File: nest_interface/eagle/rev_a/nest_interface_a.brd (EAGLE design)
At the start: 105.4 x 110.5 mm, 109 parts, among them J1 MOLEX_MICRO_USB_B_047346, J11 CONN_BLOCK_2, J12 CONN_BLOCK_2, J13 CONN_BLOCK_2, J14 CONN_BLOCK_2, J15 CONN_BLOCK_2, J17 CONN_BLOCK_3, J2 CONN_BLOCK_2, J23 CONN_BLOCK_8, J24 CONN_BLOCK_8, J25 MOLEX_MICRO_USB_B_047346, J3 CONN_BLOCK_3, J30 PINH2X12, J4 PJ-036A-SMT, J5 CONN_BLOCK_8, J6 CONN_BLOCK_8, J7 CONN_BLOCK_7, J8 CONN_BLOCK_7, U1 FT232RL, U10 ALD1107, U11 ALD1107, U2 EPIC-CORE_A, U20 MSP430F1611IPM, U3 MPC1825, U4 PCA9575, U5 PCA9575, U6 FT232RL, U7 TC1262, U8 ALD1107, U9 ALD1107, Y1 FC-135_32.768KA-A3

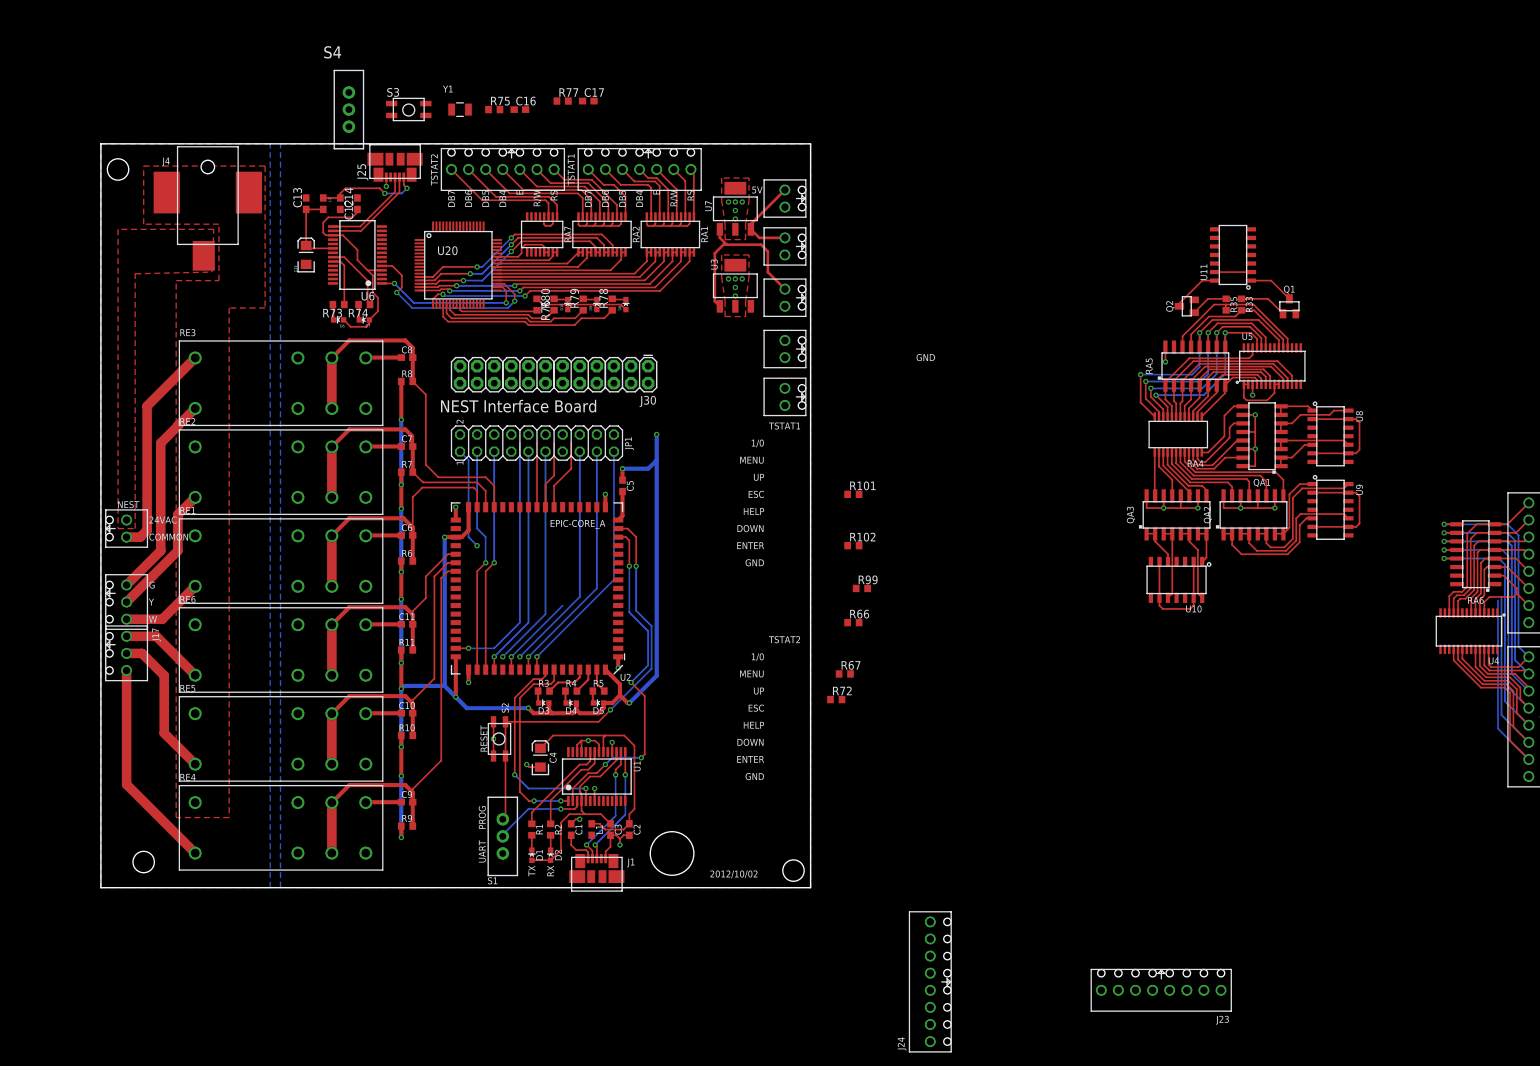
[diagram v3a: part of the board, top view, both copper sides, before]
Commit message: cleaned up the nib schematic
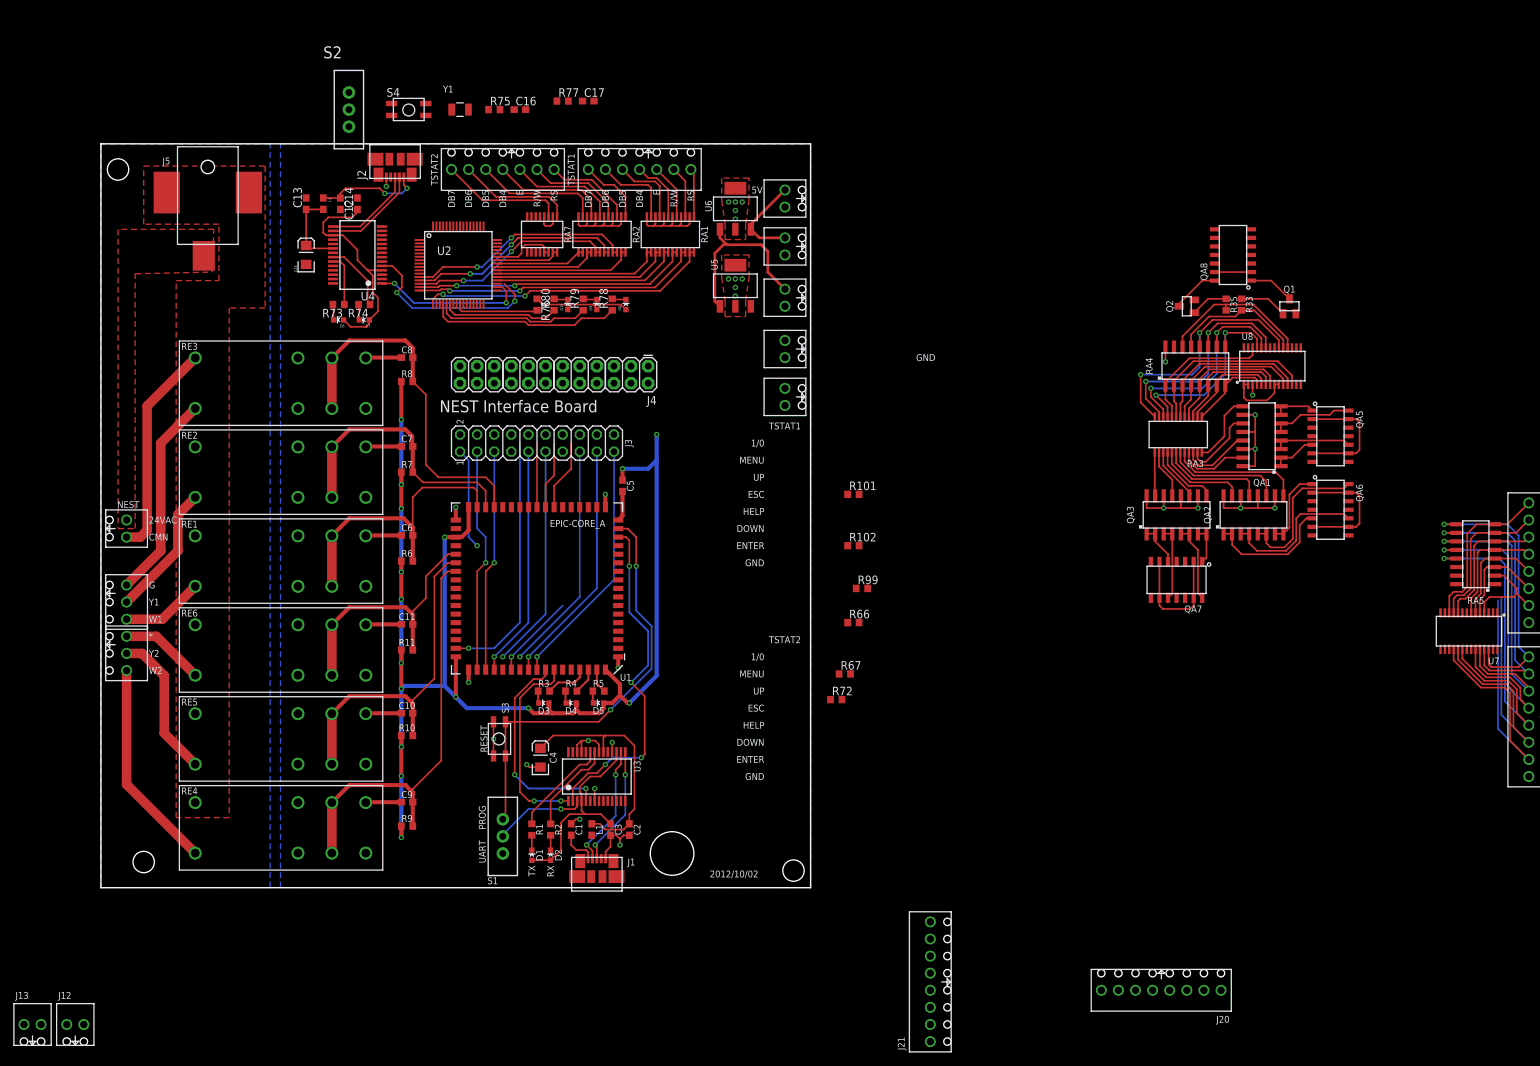
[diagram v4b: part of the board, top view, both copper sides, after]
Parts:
- removed J25: MOLEX_MICRO_USB_B_047346, nest_interface:MOLEX_MICRO_USB_B_047346
- removed J30: PINH2X12, SparkFun:2X12
- removed JP1: (no value), pinhead:2X10
- removed RA6: 766161104GP, nest_interface:SOIC-16
- removed U20: MSP430F1611IPM, hijack:PM/PAG64
- added J10, J9: CONN_BLOCK_2, nest_interface:CONN_BLOCK_2
- added J16: CONN_BLOCK_7, nest_interface:CONN_BLOCK_7
- added J18, J19: CONN_BLOCK_8, nest_interface:CONN_BLOCK_8
- added QA5: ALD1107, nest_interface:SOIC-14
- added RA3: VSSR2403103, nest_interface:LSSOP-24
- J14, J15: value CONN_BLOCK_2 -> CONN_BLOCK_3; device nest_interface:CONN_BLOCK_2 -> nest_interface:CONN_BLOCK_3
- J17: value CONN_BLOCK_3 -> CONN_BLOCK_7; device nest_interface:CONN_BLOCK_3 -> nest_interface:CONN_BLOCK_7
- J2: value CONN_BLOCK_2 -> MOLEX_MICRO_USB_B_047346; device nest_interface:CONN_BLOCK_2 -> nest_interface:MOLEX_MICRO_USB_B_047346
- J3: value CONN_BLOCK_3 -> (none); device nest_interface:CONN_BLOCK_3 -> pinhead:2X10
- J4: value PJ-036A-SMT -> PINH2X12; device nest_interface:PJ-0361-SMT -> SparkFun:2X12
- J5: value CONN_BLOCK_8 -> PJ-036A-SMT; device nest_interface:CONN_BLOCK_8 -> nest_interface:PJ-0361-SMT
- J6: value CONN_BLOCK_8 -> CONN_BLOCK_2; device nest_interface:CONN_BLOCK_8 -> nest_interface:CONN_BLOCK_2
- J7, J8: value CONN_BLOCK_7 -> CONN_BLOCK_2; device nest_interface:CONN_BLOCK_7 -> nest_interface:CONN_BLOCK_2
- RA4: value VSSR2403103 -> 766161104GP; device nest_interface:LSSOP-24 -> nest_interface:SOIC-16
- S2: value EVQP2 -> (none); device berkeley-epic:EVQP2 -> SparkFun:SWITCH-SPDT
- S4: value (none) -> EVQP2; device SparkFun:SWITCH-SPDT -> berkeley-epic:EVQP2
- U1: value FT232RL -> EPIC-CORE_A; device ftdichip:SSOP28 -> berkeley-epic:EPIC-LCC68
- U2: value EPIC-CORE_A -> MSP430F1611IPM; device berkeley-epic:EPIC-LCC68 -> hijack:PM/PAG64
- U3: value MPC1825 -> FT232RL; device nest_interface:SOT-223-3 -> ftdichip:SSOP28
- U4: value PCA9575 -> FT232RL; device nest_interface:TSSOP28 -> ftdichip:SSOP28
- U5: value PCA9575 -> MPC1825; device nest_interface:TSSOP28 -> nest_interface:SOT-223-3
- U6: value FT232RL -> TC1262; device ftdichip:SSOP28 -> nest_interface:SOT-223-3
- U7: value TC1262 -> PCA9575; device nest_interface:SOT-223-3 -> nest_interface:TSSOP28
- U8: value ALD1107 -> PCA9575; device nest_interface:SOIC-14 -> nest_interface:TSSOP28
- moved J6 210.1 mm to (3.81, 53.3), turned to 270 degrees
- moved J5 203.8 mm to (15.9, 103.3), turned to 270 degrees
- moved U4 174.3 mm to (38.1, 94.0), turned to 90 degrees
- moved J12 161.7 mm to (-3.81, -20.3), turned to 0 degrees
- moved J13 160.8 mm to (-10.2, -20.3), turned to 0 degrees
- moved U7 125.7 mm to (203.2, 38.1), turned to 180 degrees
- moved J15 104.9 mm to (3.81, 34.8), turned to 270 degrees
- moved J14 104.8 mm to (3.81, 42.4), turned to 270 degrees
- moved S2 96.1 mm to (36.8, 115.6), turned to 0 degrees
- moved S3 94.4 mm to (59.2, 22.1), turned to 270 degrees
- moved J17 91.0 mm to (59.7, 106.7), turned to 180 degrees
- moved U5 80.6 mm to (94.2, 89.4)
- moved U3 75.7 mm to (73.7, 16.5)
- moved J2 67.8 mm to (43.7, 108.2)
- moved J3 65.4 mm to (64.8, 66.0), turned to 0 degrees
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- renumbered J23 to J20, J24 to J21, U10 to QA7, U11 to QA8, U9 to QA6
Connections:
- new net TSTAT1_SPEAKER_IN: J12.2
- new net TSTAT1_SPEAKER_OUT: J12.1
- new net TSTAT2_SPEAKER_IN: J13.2
- new net TSTAT2_SPEAKER_OUT: J13.1
- net #KEYPAD_ENABLE: now also QA5.13, QA5.2, QA5.6, QA5.9, U1.P$4; no longer U2.P$4, U8.13, U8.2, U8.6, U8.9
- net 5.6V_SUPPLY: now also J7.2, U5.1, U6.1; no longer J11.2, U3.1, U7.1
- net 5V: now also J8.2, J9.2, U6.3; no longer J12.2, J13.2, U7.3
- net COMMON: now also J5.2, J5.3, J6.2; no longer J2.2, J4.2, J4.3
- net COOLING1_PIN: now also U1.P$32; no longer U2.P$32
- net COOLING2_PIN: now also U1.P$40; no longer U2.P$40
- net EPIC_ADC1: now also J3.18, U1.P$20; no longer JP1.18, U2.P$20
- net EPIC_ADC2: now also J3.16, U1.P$21; no longer JP1.16, U2.P$21
- net EPIC_ADC3: now also J3.14, U1.P$22; no longer JP1.14, U2.P$22
- net EPIC_ADC4: now also J3.12, U1.P$23; no longer JP1.12, U2.P$23
- net EPIC_ADC5: now also J3.10, U1.P$24; no longer JP1.10, U2.P$24
- net EPIC_ADC6/DAC0: now also J3.8, U1.P$25; no longer JP1.8, U2.P$25
- net EPIC_ADC7/DAC1: now also J3.6, U1.P$26; no longer JP1.6, U2.P$26
- net EPIC_MISO0: now also J3.13, U1.P$57; no longer JP1.13, U2.P$57
- net EPIC_P2.0: now also J3.1, U1.P$38; no longer JP1.1, U2.P$38
- net EPIC_P2.4: now also J3.5, U1.P$54; no longer JP1.5, U2.P$54
- net EPIC_P2.7: now also J3.3, U1.P$53; no longer JP1.3, U2.P$53
- net EPIC_P5.7: now also J3.7, U1.P$9; no longer JP1.7, U2.P$9
- net EPIC_STE0: now also J3.9, U1.P$55; no longer JP1.9, U2.P$55
- net EPIC_UART0RX: now also J3.19, U1.P$60; no longer JP1.19, U2.P$60
- net EPIC_UART0TX: now also J3.17, U1.P$59; no longer JP1.17, U2.P$59
- net FAN_PIN: now also U1.P$31; no longer U2.P$31
- net G: now also J14.1; no longer J3.1
- net GND: now also J10.1, J18.1, J19.1, J2.GND, J3.20, J7.1, J8.1, J9.1, QA5.4, RA4.16, S4.P$1, S4.P$3, U1.P$1, U1.P$18, U1.P$35, U1.P$52, U2.10, U2.11, U2.53, U2.62, U2.63, U3.18, U3.21, U3.25, U3.26, U3.7, U4.18, U4.21, U4.25, U4.26, U4.7, U5.2, U5.4, U6.2, U6.4, U7.13, U7.16, U7.17, U7.22, U8.15, U8.16, U8.22; no longer J12.1, J13.1, J14.1, J15.1, J25.GND, J5.1, J6.1, JP1.20, RA5.16, S2.P$1, S2.P$3, U1.18, U1.21, U1.25, U1.26, U1.7, U2.P$1, U2.P$18, U2.P$35, U2.P$52, U20.10, U20.11, U20.53, U20.62, U20.63, U3.2, U3.4, U4.13, U4.16, U4.17, U4.22, U5.15, U5.16, U5.22, U6.18, U6.21, U6.25, U6.26, U6.7, U7.2, U7.4, U8.4
- net HEATING1_PIN: now also U1.P$33; no longer U2.P$33
- net HEATING2_PIN: now also U1.P$41; no longer U2.P$41
- net I2C_SCL: now also J3.15, U1.P$58, U2.31, U7.28, U8.28; no longer JP1.15, U2.P$58, U20.31, U4.28, U5.28
- net I2C_SDA: now also J3.11, U1.P$56, U2.29, U7.27, U8.27; no longer JP1.11, U2.P$56, U20.29, U4.27, U5.27
- net LCDP_MISO0: now also J4.16, U2.30; no longer J30.16, U20.30
- net LCDP_P2.4: now also J4.4, U2.24; no longer J30.4, U20.24
- net LCDP_P2.7: now also U2.27; no longer U20.27
- net LCDP_STE0: now also J4.18, U2.28; no longer J30.18, U20.28
- net LCDP_URXD0: now also J4.12, U2.33; no longer J30.12, U20.33
- net LCDP_UTXD0: now also J4.14, U2.32; no longer J30.14, U20.32
- net N$10: now also U3.23; no longer U1.23
- net N$11: now also U3.22; no longer U1.22
- net N$12: now also U1.P$61, U3.5; no longer U1.5, U2.P$61
- net N$14: now also U1.P$15, U3.2; no longer U1.2, U2.P$15
- net N$15: now also U3.17, U3.4; no longer U1.17, U1.4
- net N$16: now also RA3.23; no longer RA4.23
- net N$17: now also RA3.18; no longer RA4.18
- net N$18: now also U1.P$17; no longer U2.P$17
- net N$22: now also U1.P$67; no longer U2.P$67
- net N$23: now also U1.P$66; no longer U2.P$66
- net N$24: now also U1.P$65; no longer U2.P$65
- net N$25: now also RA3.19; no longer RA4.19
- net N$26: now also RA3.20; no longer RA4.20
- net N$28: now also RA3.13; no longer RA4.13
- net N$29: now also RA3.14; no longer RA4.14
- net N$3: now also U3.16; no longer U1.16
- net N$30: now also RA3.15; no longer RA4.15
- net N$37: now also RA3.24; no longer RA4.24
- net N$38: now also U2.8; no longer U20.8
- net N$39: now also J2.VCC; no longer J25.VCC
- net N$4: now also U3.15; no longer U1.15
- net N$40: now also J2.D-, U4.16; no longer J25.D-, U6.16
- net N$41: now also J2.D+, U4.15; no longer J25.D+, U6.15
- net N$43: now also U4.20; no longer U6.20
- net N$44: now also U4.23; no longer U6.23
- net N$45: now also U4.22; no longer U6.22
- net N$48: now also U2.35, U4.1; no longer U20.34, U6.1
- net N$49: now also U2.34, U4.5; no longer U20.35, U6.5
- net N$5: now also RA3.17; no longer RA4.17
- net N$50: now also U2.57, U4.2; no longer U20.57, U6.2
- net N$51: now also U4.17, U4.4; no longer U6.17, U6.4
- net N$52: now also U2.9; no longer U20.9
- net N$54: now also U2.25; no longer U20.25
- net N$56: now also U2.21; no longer U20.21
- net N$57: now also U2.22; no longer U20.22
- net N$58: now also RA3.22; no longer RA4.22
- net N$6: now also U3.20; no longer U1.20
- net N$60: now also RA3.21; no longer RA4.21
- net N$65: now also RA3.16; no longer RA4.16
- net N$8: now also U2.20; no longer U20.20
- net N$9: now also U1.P$62, U3.1; no longer U1.1, U2.P$62
- net P1.6: now also J4.10, U2.18; no longer J30.10, U20.18
- net P1.7: now also J4.8, U2.19; no longer J30.8, U20.19
- net P2.3: now also J4.6, U2.23; no longer J30.6, U20.23
- net P2.6: now also J4.2, U2.26; no longer J30.2, U20.26
- net P5.0: now also J4.1, U2.44; no longer J30.1, U20.44
- net P5.1: now also J4.3, U2.45; no longer J30.3, U20.45
- net P5.2: now also J4.5, U2.46; no longer J30.5, U20.46
- net P5.3: now also J4.7, U2.47; no longer J30.7, U20.47
- net P5.4: now also J4.9, U2.48; no longer J30.9, U20.48
- net P5.5: now also U2.49; no longer U20.49
- net P5.6: now also J4.11, U2.50; no longer J30.11, U20.50
- net P5.7: now also J4.13, U2.51; no longer J30.13, U20.51
- net P6.0: now also J4.15, U2.59; no longer J30.15, U20.59
- net P6.1: now also J4.17, U2.60; no longer J30.17, U20.60
- net P6.2: now also J4.19, U2.61; no longer J30.19, U20.61
- net P6.3: now also J4.21, U2.2; no longer J30.21, U20.2
- net P6.4: now also J4.23, U2.3; no longer J30.23, U20.3
- net P6.5: now also J4.24, U2.4; no longer J30.24, U20.4
- net P6.6: now also J4.22, U2.5; no longer J30.22, U20.5
- net P6.7: now also J4.20, U2.6; no longer J30.20, U20.6
- net RADIO_SFD: now also J3.4, U1.P$50; no longer JP1.4, U2.P$50
- net RH: now also J5.1, J6.1; no longer J2.1, J4.1
- net RST: now also S3.P$2, S3.P$4, U1.P$16; no longer S2.P$2, S2.P$4, U2.P$16
- net RST1: now also S2.1, S4.P$2, S4.P$4, U2.58; no longer S3.P$2, S3.P$4, S4.1, U20.58
- net RST_USB: now also U3.3; no longer U1.3
- net RST_USB1: now also S2.2, U4.3; no longer S4.2, U6.3
- net STAR: now also J15.1; no longer J17.1
- net STAR_PIN: now also U1.P$39; no longer U2.P$39
- net TSTAT1_DOWN_IN: now also J18.3, RA5.3, U7.5; no longer J5.3, RA6.3, U4.5
- net TSTAT1_DOWN_OUT_PIN: now also RA3.6, RA4.3, U8.11; no longer RA4.6, RA5.3, U5.11
- net TSTAT1_ENTER_IN: now also J18.2, RA5.2, U7.4; no longer J5.2, RA6.2, U4.4
- net TSTAT1_ENTER_OUT_PIN: now also RA3.7, RA4.2, U8.12; no longer RA4.7, RA5.2, U5.12
- net TSTAT1_ESC_IN: now also J18.5, QA5.7, RA5.5, U7.7; no longer J5.5, RA6.5, U4.7, U8.7
- net TSTAT1_ESC_OUT: now also QA5.5; no longer U8.5
- net TSTAT1_ESC_OUT_PIN: now also RA3.4, RA4.5, U8.7; no longer RA4.4, RA5.5, U5.7
- net TSTAT1_HELP_IN: now also J18.4, RA5.4, U7.6; no longer J5.4, RA6.4, U4.6
- net TSTAT1_HELP_OUT_PIN: now also RA3.5, RA4.4, U8.10; no longer RA4.5, RA5.4, U5.10
- net TSTAT1_LCD_DB4: now also J16.4; no longer J7.4
- net TSTAT1_LCD_DB4_PIN: now also U2.36; no longer U20.36
- net TSTAT1_LCD_DB5: now also J16.5; no longer J7.5
- net TSTAT1_LCD_DB5_PIN: now also U2.37; no longer U20.37
- net TSTAT1_LCD_DB6: now also J16.6; no longer J7.6
- net TSTAT1_LCD_DB6_PIN: now also U2.38; no longer U20.38
- net TSTAT1_LCD_DB7: now also J16.7; no longer J7.7
- net TSTAT1_LCD_DB7_PIN: now also U2.39; no longer U20.39
- net TSTAT1_LCD_E: now also J16.3; no longer J7.3
- net TSTAT1_LCD_E_PIN: now also U2.15; no longer U20.15
- net TSTAT1_LCD_R/W: now also J16.2; no longer J7.2
- net TSTAT1_LCD_R/W_PIN: now also U2.16; no longer U20.16
- net TSTAT1_LCD_RS: now also J16.1; no longer J7.1
- net TSTAT1_LCD_RS_PIN: now also U2.17; no longer U20.17
- net TSTAT1_MENU_IN: now also J18.7, QA5.12, RA5.7, U7.11; no longer J5.7, RA6.7, U4.11, U8.12
- net TSTAT1_MENU_OUT: now also QA5.14; no longer U8.14
- net TSTAT1_MENU_OUT_PIN: now also RA3.2, RA4.7, U8.5; no longer RA4.2, RA5.7, U5.5
- net TSTAT1_ON/OFF_IN: now also J18.8, QA5.3, RA5.8, U7.12; no longer J5.8, RA6.8, U4.12, U8.3
- net TSTAT1_ON/OFF_OUT: now also QA5.1; no longer U8.1
- net TSTAT1_ON/OFF_OUT_PIN: now also RA3.1, RA4.8, U8.4; no longer RA4.1, RA5.8, U5.4
- net TSTAT1_UP_IN: now also J18.6, QA5.8, RA5.6, U7.10; no longer J5.6, RA6.6, U4.10, U8.8
- net TSTAT1_UP_OUT: now also QA5.10; no longer U8.10
- net TSTAT1_UP_OUT_PIN: now also RA3.3, RA4.6, U8.6; no longer RA4.3, RA5.6, U5.6
- net TSTAT2_DOWN_IN: now also J19.3, RA5.14, U7.19; no longer J6.3, RA6.14, U4.19
- net TSTAT2_DOWN_OUT_PIN: now also RA4.13, U8.19; no longer RA5.13, U5.19
- net TSTAT2_ENTER_IN: now also J19.2, RA5.15, U7.18; no longer J6.2, RA6.15, U4.18
- net TSTAT2_ENTER_OUT_PIN: now also RA4.14, U8.18; no longer RA5.14, U5.18
- net TSTAT2_ESC_IN: now also J19.5, RA5.12, U7.23; no longer J6.5, RA6.12, U4.23
- net TSTAT2_ESC_OUT_PIN: now also RA3.11, U8.23; no longer RA5.11, U5.23
- net TSTAT2_HELP_IN: now also J19.4, RA5.13, U7.20; no longer J6.4, RA6.13, U4.20
- net TSTAT2_HELP_OUT_PIN: now also RA3.12, U8.20; no longer RA5.12, U5.20
- net TSTAT2_LCD_DB4: now also J17.4; no longer J8.4
- net TSTAT2_LCD_DB4_PIN: now also U2.40; no longer U20.40
- net TSTAT2_LCD_DB5: now also J17.5; no longer J8.5
- net TSTAT2_LCD_DB5_PIN: now also U2.41; no longer U20.41
- net TSTAT2_LCD_DB6: now also J17.6; no longer J8.6
- net TSTAT2_LCD_DB6_PIN: now also U2.42; no longer U20.42
- net TSTAT2_LCD_DB7: now also J17.7; no longer J8.7
- net TSTAT2_LCD_DB7_PIN: now also U2.43; no longer U20.43
- net TSTAT2_LCD_E: now also J17.3; no longer J8.3
- net TSTAT2_LCD_E_PIN: now also U2.14; no longer U20.14
- net TSTAT2_LCD_R/W: now also J17.2; no longer J8.2
- net TSTAT2_LCD_R/W_PIN: now also U2.13; no longer U20.13
- net TSTAT2_LCD_RS: now also J17.1; no longer J8.1
- net TSTAT2_LCD_RS_PIN: now also U2.12; no longer U20.12
- net TSTAT2_MENU_IN: now also J19.7, RA5.10, U7.25; no longer J6.7, RA6.10, U4.25
- net TSTAT2_MENU_OUT_PIN: now also RA3.9, U8.25; no longer RA5.9, U5.25
- net TSTAT2_ON/OFF_IN: now also J19.8, RA5.9, U7.26; no longer J6.8, RA6.9, U4.26
- net TSTAT2_ON/OFF_OUT_PIN: now also RA3.8, RA4.1, U8.26; no longer RA4.8, RA5.1, U5.26
- net TSTAT2_UP_IN: now also J19.6, RA5.11, U7.24; no longer J6.6, RA6.11, U4.24
- net TSTAT2_UP_OUT_PIN: now also RA3.10, U8.24; no longer RA5.10, U5.24
- net TSTAT_IN_I2C_INT: now also U1.P$30, U7.14; no longer U2.P$30, U4.14
- net TSTAT_IN_I2C_RST: now also U1.P$2, U7.3; no longer U2.P$2, U4.3
- net TSTAT_OUT_I2C_RST: now also U1.P$3, U8.3; no longer U2.P$3, U5.3
- net VCC: now also J10.2, J11.2, J3.2, QA5.11, RA5.16, U1.P$34, U1.P$37, U1.P$51, U1.P$68, U2.1, U2.64, U5.3, U7.1, U7.15, U7.2, U7.21, U7.8, U7.9, U8.1, U8.2, U8.21, U8.8, U8.9; no longer J14.2, J15.2, JP1.2, RA6.16, U2.P$34, U2.P$37, U2.P$51, U2.P$68, U20.1, U20.64, U3.3, U4.1, U4.15, U4.2, U4.21, U4.8, U4.9, U5.1, U5.2, U5.21, U5.8, U5.9, U8.11
- net W1: now also J14.3; no longer J3.3
- net W2: now also J15.3; no longer J17.3
- net Y1: now also J14.2; no longer J3.2
- net Y2: now also J15.2; no longer J17.2
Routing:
- net N$49: track 29.6 -> 28.6 mm
- net N$48: track 23.0 -> 22.2 mm
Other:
- board text added: "*"
- board text added: "CMN"
- board text added: "W1"
- board text added: "W2"
- board text added: "Y1"
- board text added: "Y2"
- board text removed: "COMMON"
- board text removed: "W"
- board text removed: "Y"

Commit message: more schematic updates
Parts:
- renumbered R10 to R2122, R101 to R1322, R102 to R1422, R11 to R2322, R33 to R1522, R35 to R1622, R6 to R1722, R66 to R2622, R67 to R2722, R7 to R1822, R72 to R2522, R73 to R622, R74 to R722, R75 to R1222, R76 to R1122, R77 to R2822, R78 to R1022, R79 to R922, R8 to R1922, R80 to R822, R9 to R2022, R99 to R2422
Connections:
- net #KEYPAD_ENABLE: now also QA8.6, QA8.9
- net TSTAT1_SPEAKER_IN: now also QA8.7
- net TSTAT1_SPEAKER_OUT: now also QA8.5
- net TSTAT2_SPEAKER_IN: now also QA8.8
- net TSTAT2_SPEAKER_OUT: now also QA8.10

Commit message: MOAR ROUTING
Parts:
- moved J13 219.5 mm to (188.2, 73.7), turned to 90 degrees
- moved J12 217.1 mm to (188.2, 81.0), turned to 90 degrees
- moved J21 54.5 mm to (174.2, 5.08), turned to 0 degrees
- moved QA6 28.1 mm to (168.7, 31.8), turned to 180 degrees
- moved J18 24.7 mm to (188.2, 41.9)
- moved J19 24.7 mm to (188.2, 19.1)
- moved RA5 24.7 mm to (180.3, 43.2)
- moved U7 24.7 mm to (179.3, 31.8)
- moved J20 21.4 mm to (150.9, 5.08), turned to 0 degrees
- moved QA1 14.2 mm to (169.9, 53.1)
- moved R1522 14.2 mm to (166.9, 72.6)
- moved RA3 14.2 mm to (157.5, 53.3)
- moved U8 14.2 mm to (171.4, 63.5)
- moved Q1 14.2 mm to (174.0, 72.4)
- moved Q2 14.2 mm to (158.8, 72.4)
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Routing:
- net TSTAT2_DOWN_OUT: track 6.84 -> 106.1 mm, vias 0 -> 1
- net VCC: track 231.9 -> 318.1 mm, vias 16 -> 26
- net TSTAT2_ENTER_OUT: track 7.12 -> 91.5 mm, vias 0 -> 1
- net #KEYPAD_ENABLE: track 60.7 -> 141.9 mm, vias 0 -> 5
- net TSTAT1_ON/OFF_OUT: track 6.23 -> 82.6 mm, vias 0 -> 3
- net TSTAT1_MENU_OUT: track 12.1 -> 85.1 mm, vias 0 -> 3
- net TSTAT1_ESC_OUT: track 6.76 -> 77.4 mm, vias 0 -> 2
- net TSTAT1_UP_OUT: track 11.6 -> 81.1 mm, vias 0 -> 3
- net TSTAT2_ENTER_IN: track 48.6 -> 110.9 mm, vias 0 -> 3
- net TSTAT2_DOWN_IN: track 43.5 -> 101.7 mm, vias 0 -> 3
- net TSTAT1_HELP_OUT: track 11.5 -> 65.6 mm, vias 0 -> 2
- net TSTAT1_DOWN_OUT: track 22.6 -> 69.2 mm, vias 0 -> 2
- net TSTAT2_MENU_OUT: track 5.72 -> 50.8 mm
- net TSTAT2_HELP_OUT: track 6.25 -> 51.0 mm
- net TSTAT1_ENTER_OUT: track 22.3 -> 66.3 mm, vias 0 -> 2
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
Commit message: no airwires!!!!!
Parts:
- J4: value PINH2X12 -> (none); device SparkFun:2X12 -> pinhead:2X10
- moved QA5 62.2 mm to (117.9, 51.8)
- moved R1622 62.2 mm to (102.4, 71.4)
- moved U7 62.2 mm to (117.1, 30.5)
- moved J20 62.2 mm to (88.6, 3.81)
- moved J21 62.2 mm to (112.0, 3.81)
- moved Q1 62.2 mm to (111.8, 71.1)
- moved Q2 62.2 mm to (96.5, 71.1)
- moved QA2 62.2 mm to (106.4, 40.1)
- moved QA3 62.2 mm to (95.0, 40.1)
- moved QA6 62.2 mm to (106.4, 30.5)
- moved QA7 62.2 mm to (95.0, 30.5)
- moved QA8 62.2 mm to (103.4, 78.7)
- moved RA4 62.2 mm to (97.8, 62.2)
- moved RA5 62.2 mm to (118.1, 41.9)
- moved QA1 62.2 mm to (107.7, 51.8)
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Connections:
- net LCDP_MISO0: no longer J4.16
- net LCDP_P2.4: no longer J4.4
- net LCDP_STE0: no longer J4.18
- net LCDP_URXD0: no longer J4.12
- net LCDP_UTXD0: no longer J4.14
- net P1.6: no longer J4.10
- net P1.7: no longer J4.8
- net P2.3: no longer J4.6
- net P2.6: no longer J4.2
- net P5.0: no longer J4.1
- net P5.1: no longer J4.3
- net P5.2: no longer J4.5
- net P5.3: no longer J4.7
- net P5.4: no longer J4.9
- net P5.6: no longer J4.11
- net P5.7: no longer J4.13
- net P6.0: no longer J4.15
- net P6.1: no longer J4.17
- net P6.2: no longer J4.19
- net P6.3: no longer J4.21
- net P6.4: no longer J4.23
- net P6.5: no longer J4.24
- net P6.6: no longer J4.22
- net P6.7: no longer J4.20
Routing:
- net VCC: track 318.1 -> 605.9 mm, vias 26 -> 35
- net I2C_SDA: track 45.0 -> 211.5 mm, vias 2 -> 8
- net I2C_SCL: track 47.3 -> 203.4 mm, vias 2 -> 8
- net TSTAT_IN_I2C_INT: track 0.00 -> 71.9 mm, vias 0 -> 3
- net GND: track 152.7 -> 224.1 mm, vias 31 -> 52
- net TSTAT_IN_I2C_RST: track 0.00 -> 70.7 mm, vias 0 -> 3
- net #KEYPAD_ENABLE: track 141.9 -> 197.0 mm, vias 5 -> 7
- net RST1: track 0.00 -> 53.7 mm, vias 0 -> 2
- net TSTAT_OUT_I2C_RST: track 1.62 -> 49.4 mm, vias 1 -> 4
- net EPIC_P5.7: track 0.00 -> 34.0 mm, vias 0 -> 1
- net RST_USB1: track 0.00 -> 27.4 mm, vias 0 -> 1
- net EPIC_MISO0: track 12.7 -> 35.5 mm
- net N$50: track 0.00 -> 17.9 mm, vias 0 -> 2
- net 5.6V_SUPPLY: track 26.4 -> 39.5 mm
- net EPIC_ADC1: track 0.00 -> 12.4 mm
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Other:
- board size 105.4 x 110.5 mm -> 133.3 x 110.5 mm
- board text added: "3V"
- board text added: "5.6V"
- board text added: "SPEAKER_IN"
- board text added: "SPEAKER_OUT"
- board text added: "TSTAT1_IN"
- board text added: "TSTAT1_OUT"
- board text added: "TSTAT2_IN"
- board text added: "TSTAT2_OUT"
